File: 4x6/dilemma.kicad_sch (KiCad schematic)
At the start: 320 parts, among them J1 USB_C_Receptacle_USB2.0, J102 NA_serial, J105 NA_Conn_01x04_Female, J113 Cirque, J3 NA_GC9A01, J4 Conn_01x05, J5 NA_Conn_01x02, J5001 USB_C_Receptacle_USB2.0, J5002 NA_Conn_01x02, J5003 NA_serial, J5004 NA_GC9A01, J5005 NA_Conn_01x04_Female, J5007 Cirque, J5008 Conn_01x05, J5009 Conn_01x05, J5010 Conn_01x05, SW1 SW_Push, SW101 NA_SW_Push, SW102 NA_SW_Push, SW103 NA_SW_Push, SW104 NA_SW_Push, SW105 NA_SW_Push, SW106 NA_SW_Push, SW107 NA_SW_Push, SW108 NA_SW_Push, SW109 NA_SW_Push, SW112 NA_SW_Push, SW113 NA_SW_Push, SW114 NA_SW_Push, SW115 NA_SW_Push, SW116 NA_SW_Push, SW117 NA_SW_Push, SW118 NA_SW_Push, SW119 NA_SW_Push, SW3001 NA_SW_Push, SW3002 NA_RotaryEncoder_Switch, SW5001 SW_Push, SW5002 NA_SW_Push, SW5003 NA_SW_Push, SW5004 NA_SW_Push, SW5005 NA_SW_Push, SW5006 NA_SW_Push, SW5007 NA_SW_Push, SW5008 NA_SW_Push, SW5009 NA_SW_Push, SW5010 NA_SW_Push, SW5011 NA_SW_Push, SW5012 NA_SW_Push, SW5013 NA_SW_Push, SW5014 NA_SW_Push, SW5015 NA_SW_Push, SW5016 NA_SW_Push, SW5017 NA_SW_Push, SW5018 NA_SW_Push, SW5019 NA_SW_Push, SW5020 NA_RotaryEncoder_Switch, SW5021 SW_SPST, SW5022 SW_SPST, SW5023 NA_SW_Push, SW5024 NA_SW_Push, SW5025 NA_SW_Push, SW5026 NA_SW_Push, SW5027 NA_SW_Push, SW5028 NA_SW_Push, SW5029 NA_SW_Push, SW5030 NA_SW_Push, SW5031 NA_SW_Push, SW5032 NA_SW_Push, SW5033 NA_SW_Push, SW5034 NA_SW_Push, SW5035 NA_SW_Push, SW5036 NA_SW_Push, SW5037 NA_SW_Push, SW5038 NA_SW_Push, SW5039 NA_SW_Push, SW5040 NA_SW_Push, SW5041 NA_SW_Push, U1 RP2040, U2 W25Q128JVS, U3 XC6210B332MR-G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

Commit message: left per key rgb
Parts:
- removed D5126: D_matrix, local-libraries:D_0402, symbol Device:D
- removed D5127: SK6812MINI, local-libraries:SK6812_mini_e_corners, symbol LED:SK6812MINI
- removed SW5041: NA_SW_Push, local-libraries:SW_MX_choc, symbol Switch:SW_Push
- added D5128, D5129, D5130, D5131, D5132, D5133, D5134, D5135, D5136: SK6812MINI, local-libraries:SK6812_mini_e_corners, symbol LED:SK6812MINI
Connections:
- net +3V3_L: now also D5128.4 (VDD), D5129.4 (VDD), D5130.4 (VDD), D5131.4 (VDD), D5132.4 (VDD), D5133.4 (VDD), D5134.4 (VDD), D5135.4 (VDD), D5136.4 (VDD)
- net GND_L: now also D5128.2 (VSS), D5129.2 (VSS), D5130.2 (VSS), D5131.2 (VSS), D5132.2 (VSS), D5133.2 (VSS), D5134.2 (VSS), D5135.2 (VSS), D5136.2 (VSS)
- net RGB_L: no longer D5049.3 (DIN)
- net at D5064.1 (DOUT): now also D5062.3 (DIN); no longer D5050.3 (DIN)
- net at D5064.3 (DIN): now also D5050.1 (DOUT); no longer D5062.1 (DOUT)
- net at D5052.1 (DOUT): now also D5049.3 (DIN); no longer D5054.3 (DIN)
- net at D5052.3 (DIN): now also D5054.1 (DOUT); no longer D5049.1 (DOUT)
- net at D5058.1 (DOUT): now also D5056.3 (DIN); no longer D5060.3 (DIN)
- net at D5058.3 (DIN): now also D5134.1 (DOUT); no longer D5056.1 (DOUT)
- net at D5065.3 (DIN): now also D5055.1 (DOUT); no longer D5063.1 (DOUT)
- net at D5057.3 (DIN): now also D5059.1 (DOUT); no longer D5055.1 (DOUT)
- net at D5055.3 (DIN): now also D5057.1 (DOUT); no longer D5053.1 (DOUT)
- net at D5061.3 (DIN): now also D5063.1 (DOUT); no longer D5059.1 (DOUT)
- net at D5059.3 (DIN): now also D5061.1 (DOUT); no longer D5057.1 (DOUT)
- net at D5053.3 (DIN): now also D5049.1 (DOUT); no longer D5050.1 (DOUT)
- net at D5060.1 (DOUT): now also D5135.3 (DIN); no longer D5062.3 (DIN)
- net at D5063.3 (DIN): now also D5136.1 (DOUT); no longer D5061.1 (DOUT)
- new net: D5132.1 (DOUT), D5133.3 (DIN)
- new net: D5131.1 (DOUT), D5132.3 (DIN)
- new net: D5135.1 (DOUT), D5136.3 (DIN)
- new net: D5133.1 (DOUT), D5134.3 (DIN)
- new net: D5050.3 (DIN), D5053.1 (DOUT)
- new net: D5128.1 (DOUT), D5129.3 (DIN)
- new net: D5054.3 (DIN), D5056.1 (DOUT)
- new net: D5060.3 (DIN), D5062.1 (DOUT)
- new net: D5130.1 (DOUT), D5131.3 (DIN)
- new net: D5129.1 (DOUT), D5130.3 (DIN)
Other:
- note added: "Per-key RGB"
- note removed: "Per key RGB"
- moved on the sheet: C5017, C5018, D5031, D5032, D5033, D5034, D5035, D5036, D5037, D5038, D5039, D5040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

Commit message: cleanup
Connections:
- net M_COL6: now also U1.17 (GPIO14)
- net M_COL6_L: now also U5002.17 (GPIO14)
- net M_ROW5: now also U1.18 (GPIO15)
- net M_ROW5_L: now also U5002.18 (GPIO15)
- net RGB_L: now also D5128.3 (DIN)
- net at D27.3 (DOUT): now also D4.1 (DIN)
- net IO16_L: now reaches U5002.27 (GPIO16)
- net IO16_L: now also J5008.2 (Pin_2), J5009.2 (Pin_2)
- net IO18_L: now reaches U5002.29 (GPIO18)
- net IO18_L: now also J5008.3 (Pin_3), J5009.3 (Pin_3)
- removed net IO14_L: J5008.2 (Pin_2), J5009.2 (Pin_2), U5002.17 (GPIO14)
- removed net IO15_L: J5008.3 (Pin_3), J5009.3 (Pin_3), U5002.18 (GPIO15)
- no-connect marks 27 -> 23
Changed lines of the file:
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@@
   )
   (no_connect (at 833.755 222.25))
-  (no_connect (at 180.34 394.335))
   (no_connect (at 342.265 50.8))
   (no_connect (at 342.265 40.64))
@@
   (no_connect (at 342.265 45.72))
   (no_connect (at 262.89 471.805))
-  (no_connect (at 182.88 93.98))
-  (no_connect (at 182.88 96.52))
   (no_connect (at 182.88 58.42))
   (no_connect (at 339.725 346.075))
   (no_connect (at 339.725 335.915))
   (no_connect (at 48.26 360.045))
-  (no_connect (at 180.34 399.415))
   (no_connect (at 339.725 338.455))
   (no_connect (at 657.86 307.34))
@@
     (stroke (width 0) (type default))
   )
+  (wire (pts (xy 394.97 45.72) (xy 584.835 45.72))
+    (stroke (width 0) (type default))
+  )
   (wire (pts (xy 196.85 528.32) (xy 196.85 538.48))
     (stroke (width 0) (type default))
@@
     (stroke (width 0) (type default))
   )
-  (wire (pts (xy 394.97 45.72) (xy 565.785 45.72))
-    (stroke (width 0) (type default))
-  )
   (wire (pts (xy 153.67 231.14) (xy 153.67 228.6))
     (stroke (width 0) (type default))
@@
     )
   )
+  (global_label "M_COL6_L" (shape input) (at 180.34 389.255 0)
+    (effects (font (size 1.27 1.27)) (justify left))
+    (property "Intersheetrefs" "${INTERSHEET_REFS}" (at 205.105 58.42 0)
+      (effects (font (size 1.27 1.27)) hide)
+    )
+  )
   (global_label "SERIAL" (shape input) (at 265.43 179.07 0)
     (effects (font (size 1.27 1.27)) (justify left))
@@
     )
   )
-  (global_label "IO15_L" (shape input) (at 436.88 433.07 180) (fields_autoplaced)
+  (global_label "IO18_L" (shape input) (at 436.88 433.07 180) (fields_autoplaced)
     (effects (font (size 1.27 1.27)) (justify right))
     (property "Intersheetrefs" "${INTERSHEET_REFS}" (at 428.1169 432.9906 0)
@@
     )
   )
-  (global_label "IO14_L" (shape input) (at 434.34 407.67 180) (fields_autoplaced)
+  (global_label "IO16_L" (shape input) (at 434.34 407.67 180) (fields_autoplaced)
     (effects (font (size 1.27 1.27)) (justify right))
     (property "Intersheetrefs" "${INTERSHEET_REFS}" (at 425.5769 407.5906 0)
@@
     )
   )
+  (global_label "RGB_L" (shape input) (at 798.195 328.93 0)
+    (effects (font (size 1.27 1.27)) (justify left))
+    (property "Intersheetrefs" "${INTERSHEET_REFS}" (at 885.825 396.24 0)
+      (effects (font (size 1.27 1.27)) hide)
+    )
+  )
   (global_label "SCL_L" (shape input) (at 180.34 361.315 0)
     (effects (font (size 1.27 1.27)) (justify left))
@@
     )
   )
+  (global_label "M_ROW5" (shape input) (at 182.88 96.52 0)
+    (effects (font (size 1.27 1.27)) (justify left))
+    (property "Intersheetrefs" "${INTERSHEET_REFS}" (at 212.09 156.21 0)
+      (effects (font (size 1.27 1.27)) hide)
+    )
+  )
   (global_label "M_ROW3" (shape input) (at 35.56 238.76 180)
     (effects (font (size 1.27 1.27)) (justify right))
@@
     )
   )
-  (global_label "IO15_L" (shape input) (at 434.34 410.21 180) (fields_autoplaced)
+  (global_label "IO18_L" (shape input) (at 434.34 410.21 180) (fields_autoplaced)
     (effects (font (size 1.27 1.27)) (justify right))
     (property "Intersheetrefs" "${INTERSHEET_REFS}" (at 425.5769 410.1306 0)
@@
     )
   )
-  (global_label "IO14_L" (shape input) (at 436.88 430.53 180) (fields_autoplaced)
+  (global_label "IO16_L" (shape input) (at 436.88 430.53 180) (fields_autoplaced)
     (effects (font (size 1.27 1.27)) (justify right))
     (property "Intersheetrefs" "${INTERSHEET_REFS}" (at 428.1169 430.4506 0)
@@
     )
   )
-  (global_label "IO15_L" (shape input) (at 180.34 391.795 0) (fields_autoplaced)
+  (global_label "IO18_L" (shape input) (at 180.34 399.415 0) (fields_autoplaced)
     (effects (font (size 1.27 1.27)) (justify left))
-    (property "Intersheetrefs" "${INTERSHEET_REFS}" (at 189.1031 391.7156 0)
+    (property "Intersheetrefs" "${INTERSHEET_REFS}" (at 189.1031 399.3356 0)
       (effects (font (size 1.27 1.27)) (justify left) hide)
     )
@@
     )
   )
-  (global_label "IO14_L" (shape input) (at 180.34 389.255 0) (fields_autoplaced)
+  (global_label "IO16_L" (shape input) (at 180.34 394.335 0) (fields_autoplaced)
     (effects (font (size 1.27 1.27)) (justify left))
-    (property "Intersheetrefs" "${INTERSHEET_REFS}" (at 189.1031 389.1756 0)
+    (property "Intersheetrefs" "${INTERSHEET_REFS}" (at 189.1031 394.2556 0)
       (effects (font (size 1.27 1.27)) (justify left) hide)
     )
@@
     )
   )
+  (global_label "M_ROW5_L" (shape input) (at 180.34 391.795 0)
+    (effects (font (size 1.27 1.27)) (justify left))
+    (property "Intersheetrefs" "${INTERSHEET_REFS}" (at 252.095 438.15 0)
+      (effects (font (size 1.27 1.27)) hide)
+    )
+  )
   (global_label "M_COL1_L" (shape input) (at 180.34 374.015 0)
     (effects (font (size 1.27 1.27)) (justify left))
@@
     )
   )
+  (global_label "M_COL6" (shape input) (at 182.88 93.98 0)
+    (effects (font (size 1.27 1.27)) (justify left))
+    (property "Intersheetrefs" "${INTERSHEET_REFS}" (at 212.09 153.67 0)
+      (effects (font (size 1.27 1.27)) hide)
+    )
+  )
   (global_label "M_COL4" (shape input) (at 182.88 73.66 0)
     (effects (font (size 1.27 1.27)) (justify left))
@@
   (symbol (lib_id "power:+3.3V") (at 790.575 60.325 180) (unit 1)
     (in_bom yes) (on_board yes) (dnp no)
-    (property "Reference" "#PWR?" (at 790.575 56.515 0)
+    (property "Reference" "#PWR0129" (at 790.575 56.515 0)
       (effects (font (size 1.27 1.27)) hide)
     )
@@
       (project "dilemma"
         (path "/7353e96a-343a-4876-b497-b1d205a14d97"
-          (reference "#PWR?") (unit 1)
+          (reference "#PWR0129") (unit 1)
         )
       )

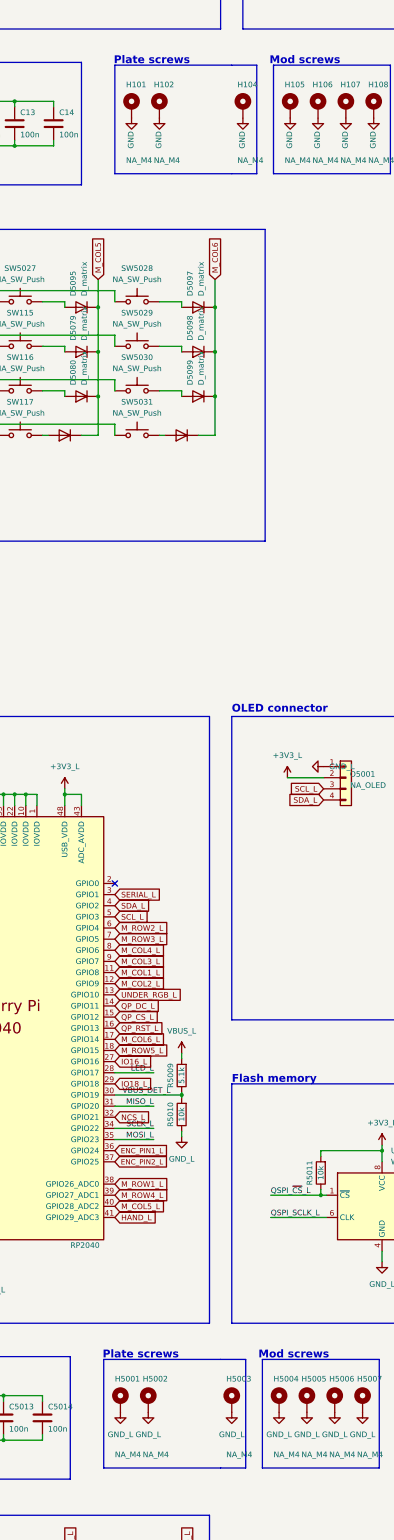
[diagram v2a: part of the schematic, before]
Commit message: add screws
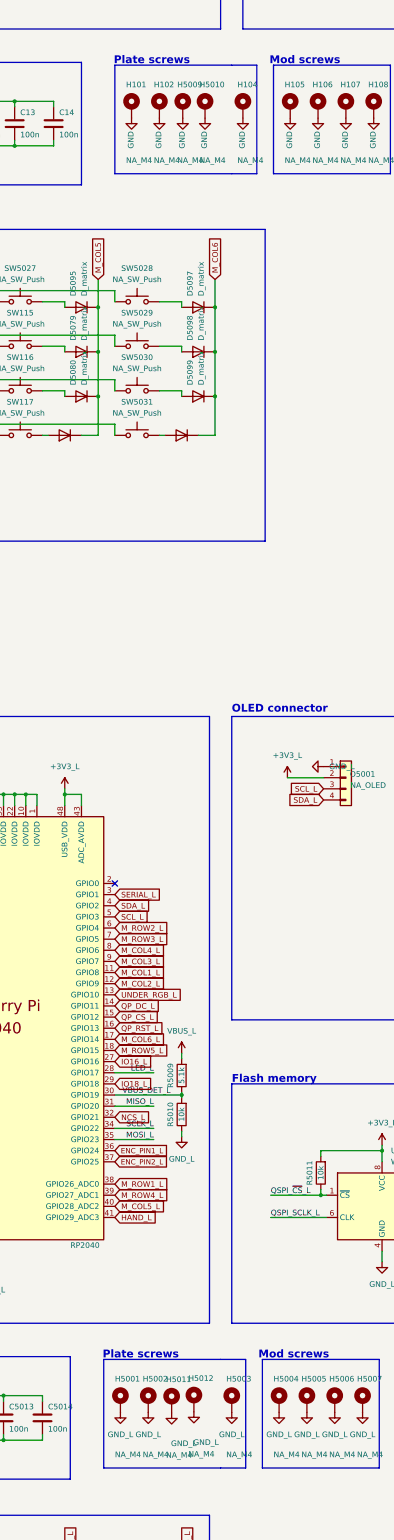
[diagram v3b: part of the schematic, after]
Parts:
- added H5009, H5010, H5011, H5012: NA_M4, local-libraries:MountingHole_3mm_Pad_Via, symbol Mechanical:MountingHole_Pad
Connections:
- net GND: now also H5009.1, H5010.1, H5011.1, H5012.1
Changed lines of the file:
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@@
     )
   )
+  (symbol (lib_id "Mechanical:MountingHole_Pad") (at 195.834 176.53 0) (unit 1)
+    (in_bom yes) (on_board yes) (dnp no)
+    (property "Reference" "H5009" (at 194.564 171.45 0)
+      (effects (font (size 1.27 1.27)) (justify left))
+    )
+    (property "Value" "NA_M4" (at 194.564 188.722 0)
+      (effects (font (size 1.27 1.27)) (justify left))
+    )
+    (property "Footprint" "local-libraries:MountingHole_3mm_Pad_Via" (at 195.834 176.53 0)
+      (effects (font (size 1.27 1.27)) hide)
+    )
+    (property "Datasheet" "~" (at 195.834 176.53 0)
+      (effects (font (size 1.27 1.27)) hide)
+    )
+    (pin "1")
+    (instances
+      (project "dilemma"
+        (path "/7353e96a-343a-4876-b497-b1d205a14d97"
+          (reference "H5009") (unit 1)
+        )
+      )
+    )
+  )
   (symbol (lib_id "Regulator_Linear:AP2127K-3.3") (at 46.99 115.57 0) (unit 1)
     (in_bom yes) (on_board yes) (dnp no)
@@
     )
   )
+  (symbol (lib_id "Mechanical:MountingHole_Pad") (at 198.374 471.678 0) (unit 1)
+    (in_bom yes) (on_board yes) (dnp no)
+    (property "Reference" "H5012" (at 197.104 466.598 0)
+      (effects (font (size 1.27 1.27)) (justify left))
+    )
+    (property "Value" "NA_M4" (at 197.104 483.87 0)
+      (effects (font (size 1.27 1.27)) (justify left))
+    )
+    (property "Footprint" "local-libraries:MountingHole_3mm_Pad_Via" (at 198.374 471.678 0)
+      (effects (font (size 1.27 1.27)) hide)
+    )
+    (property "Datasheet" "~" (at 198.374 471.678 0)
+      (effects (font (size 1.27 1.27)) hide)
+    )
+    (pin "1")
+    (instances
+      (project "dilemma"
+        (path "/7353e96a-343a-4876-b497-b1d205a14d97"
+          (reference "H5012") (unit 1)
+        )
+      )
+    )
+  )
   (symbol (lib_id "Device:D") (at 199.39 222.25 180) (unit 1)
     (in_bom yes) (on_board yes) (dnp no)
@@
     )
   )
+  (symbol (lib_id "power:GND") (at 198.374 474.218 0) (unit 1)
+    (in_bom yes) (on_board yes) (dnp no)
+    (property "Reference" "#PWR05173" (at 198.374 480.568 0)
+      (effects (font (size 1.27 1.27)) hide)
+    )
+    (property "Value" "GND_L" (at 198.218 481.2029 0)
+      (effects (font (size 1.27 1.27)) (justify left))
+    )
+    (property "Footprint" "" (at 198.374 474.218 0)
+      (effects (font (size 1.27 1.27)) hide)
+    )
+    (property "Datasheet" "" (at 198.374 474.218 0)
+      (effects (font (size 1.27 1.27)) hide)
+    )
+    (pin "1")
+    (instances
+      (project "dilemma"
+        (path "/7353e96a-343a-4876-b497-b1d205a14d97"
+          (reference "#PWR05173") (unit 1)
+        )
+      )
+    )
+  )
   (symbol (lib_id "power:GND") (at 790.575 85.725 0) (unit 1)
     (in_bom yes) (on_board yes) (dnp no)
@@
     )
   )
+  (symbol (lib_id "power:GND") (at 200.914 179.07 0) (unit 1)
+    (in_bom yes) (on_board yes) (dnp no)
+    (property "Reference" "#PWR05118" (at 200.914 185.42 0)
+      (effects (font (size 1.27 1.27)) hide)
+    )
+    (property "Value" "GND" (at 200.758 186.0549 90)
+      (effects (font (size 1.27 1.27)) (justify left))
+    )
+    (property "Footprint" "" (at 200.914 179.07 0)
+      (effects (font (size 1.27 1.27)) hide)
+    )
+    (property "Datasheet" "" (at 200.914 179.07 0)
+      (effects (font (size 1.27 1.27)) hide)
+    )
+    (pin "1")
+    (instances
+      (project "dilemma"
+        (path "/7353e96a-343a-4876-b497-b1d205a14d97"
+          (reference "#PWR05118") (unit 1)
+        )
+      )
+    )
+  )
   (symbol (lib_id "power_L:+3V3_L") (at 663.575 273.05 180) (unit 1)
     (in_bom yes) (on_board yes) (dnp no)
@@
     )
   )
+  (symbol (lib_id "power:GND") (at 193.294 474.472 0) (unit 1)
+    (in_bom yes) (on_board yes) (dnp no)
+    (property "Reference" "#PWR05172" (at 193.294 480.822 0)
+      (effects (font (size 1.27 1.27)) hide)
+    )
+    (property "Value" "GND_L" (at 193.138 481.4569 0)
+      (effects (font (size 1.27 1.27)) (justify left))
+    )
+    (property "Footprint" "" (at 193.294 474.472 0)
+      (effects (font (size 1.27 1.27)) hide)
+    )
+    (property "Datasheet" "" (at 193.294 474.472 0)
+      (effects (font (size 1.27 1.27)) hide)
+    )
+    (pin "1")
+    (instances
+      (project "dilemma"
+        (path "/7353e96a-343a-4876-b497-b1d205a14d97"
+          (reference "#PWR05172") (unit 1)
+        )
+      )
+    )
+  )
   (symbol (lib_id "Switch:SW_Push") (at 52.07 220.98 0) (unit 1)
     (in_bom yes) (on_board yes) (dnp no)
@@
     )
   )
+  (symbol (lib_id "power:GND") (at 195.834 179.07 0) (unit 1)
+    (in_bom yes) (on_board yes) (dnp no)
+    (property "Reference" "#PWR05065" (at 195.834 185.42 0)
+      (effects (font (size 1.27 1.27)) hide)
+    )
+    (property "Value" "GND" (at 195.678 186.0549 90)
+      (effects (font (size 1.27 1.27)) (justify left))
+    )
+    (property "Footprint" "" (at 195.834 179.07 0)
+      (effects (font (size 1.27 1.27)) hide)
+    )
+    (property "Datasheet" "" (at 195.834 179.07 0)
+      (effects (font (size 1.27 1.27)) hide)
+    )
+    (pin "1")
+    (instances
+      (project "dilemma"
+        (path "/7353e96a-343a-4876-b497-b1d205a14d97"
+          (reference "#PWR05065") (unit 1)
+        )
+      )
+    )
+  )
   (symbol (lib_id "Device:C") (at 101.6 180.34 0) (unit 1)
     (in_bom yes) (on_board yes) (dnp no)
@@
     )
   )
+  (symbol (lib_id "Mechanical:MountingHole_Pad") (at 200.914 176.53 0) (unit 1)
+    (in_bom yes) (on_board yes) (dnp no)
+    (property "Reference" "H5010" (at 199.644 171.45 0)
+      (effects (font (size 1.27 1.27)) (justify left))
+    )
+    (property "Value" "NA_M4" (at 199.644 188.722 0)
+      (effects (font (size 1.27 1.27)) (justify left))
+    )
+    (property "Footprint" "local-libraries:MountingHole_3mm_Pad_Via" (at 200.914 176.53 0)
+      (effects (font (size 1.27 1.27)) hide)
+    )
+    (property "Datasheet" "~" (at 200.914 176.53 0)
+      (effects (font (size 1.27 1.27)) hide)
+    )
+    (pin "1")
+    (instances
+      (project "dilemma"
+        (path "/7353e96a-343a-4876-b497-b1d205a14d97"
+          (reference "H5010") (unit 1)
+        )
+      )
+    )
+  )
   (symbol (lib_id "power_L:GND_L") (at 52.705 481.33 0) (unit 1)
     (in_bom yes) (on_board yes) (dnp no) (fields_autoplaced)
@@
         )
       )
+    )
+  )
+  (symbol (lib_id "Mechanical:MountingHole_Pad") (at 193.294 471.932 0) (unit 1)
+    (in_bom yes) (on_board yes) (dnp no)
+    (property "Reference" "H5011" (at 192.024 466.852 0)
+      (effects (font (size 1.27 1.27)) (justify left))
+    )
+    (property "Value" "NA_M4" (at 192.024 484.124 0)
+      (effects (font (size 1.27 1.27)) (justify left))
+    )
+    (property "Footprint" "local-libraries:MountingHole_3mm_Pad_Via" (at 193.294 471.932 0)
+      (effects (font (size 1.27 1.27)) hide)
+    )
+    (property "Datasheet" "~" (at 193.294 471.932 0)
+      (effects (font (size 1.27 1.27)) hide)
+    )
+    (pin "1")
+    (instances
+      (project "dilemma"
+        (path "/7353e96a-343a-4876-b497-b1d205a14d97"
+          (reference "H5011") (unit 1)
+        )
+      )
